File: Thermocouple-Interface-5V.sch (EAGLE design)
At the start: 16 parts, among them U1 MAX31855, U3 LP298XS

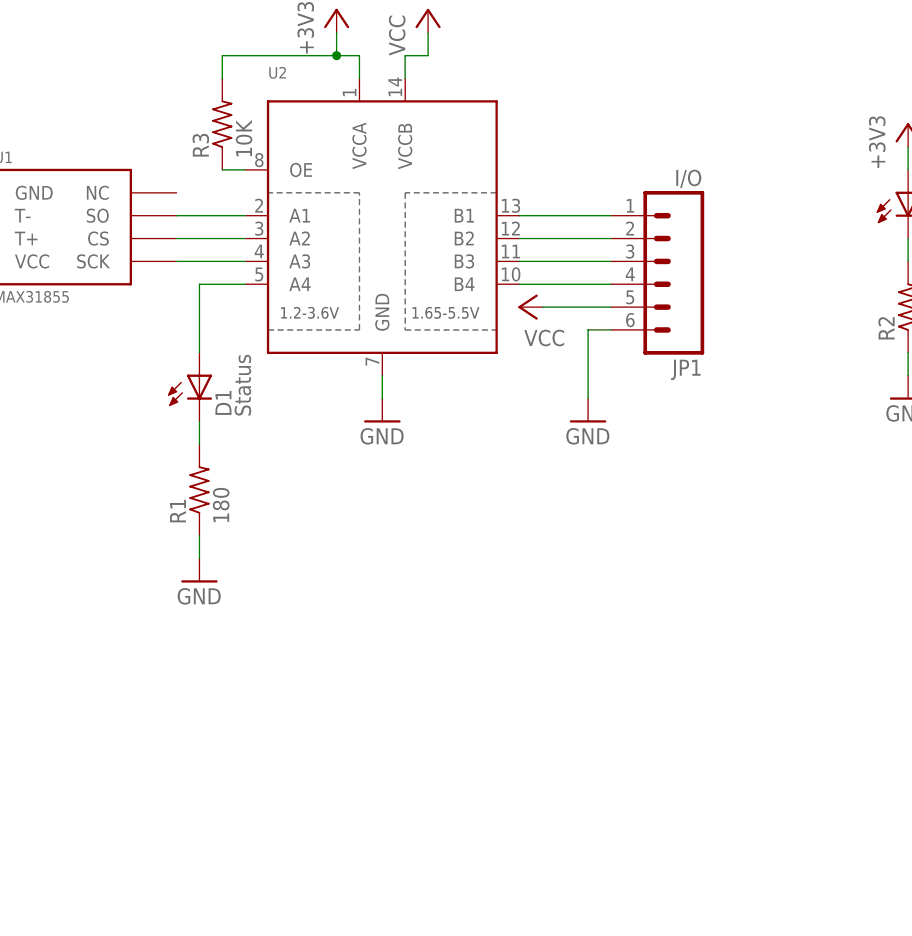
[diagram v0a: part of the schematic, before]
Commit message: Status led no longer routes through level shifter, bumped to v2.0.1 for 01-2012 pcb production
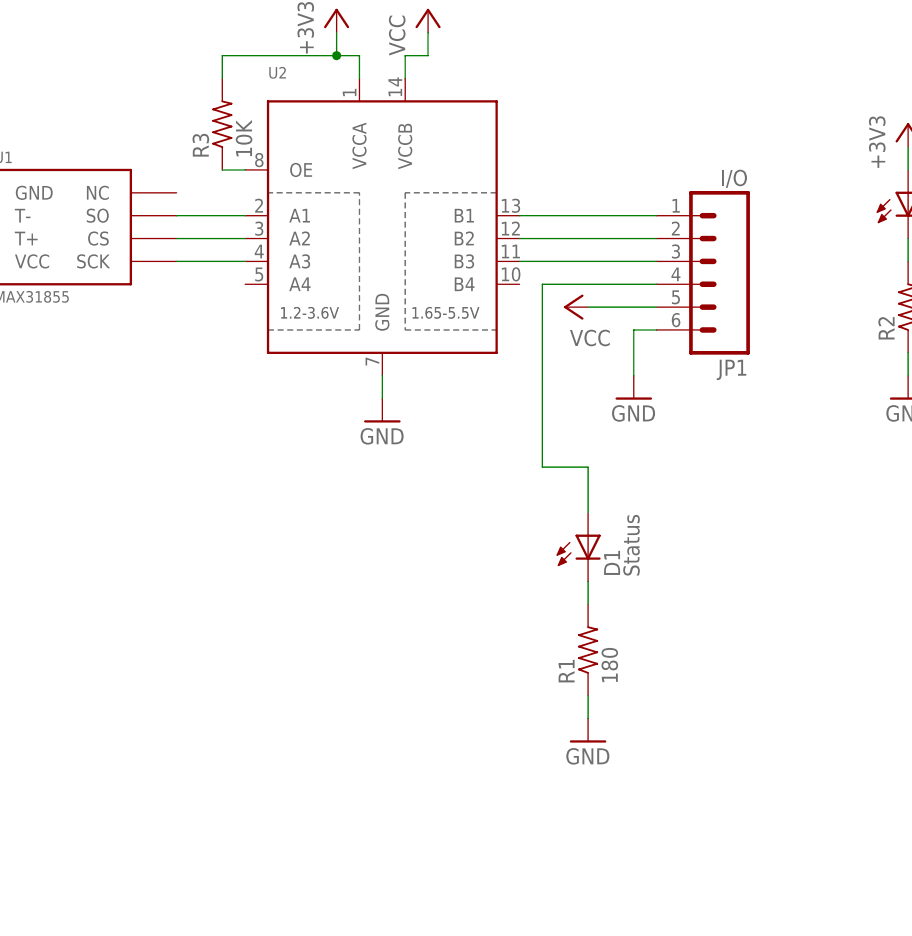
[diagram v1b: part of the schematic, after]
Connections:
- removed net STATUS: D1.A, U2.A4
- removed net _STATUS: JP1.4, U2.B4
- new net N$4: D1.A, JP1.4
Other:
- moved on the sheet: D1, JP1, R1
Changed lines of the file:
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@@
 <instance part="TC1" gate="G$1" x="78.74" y="124.46" rot="R180"/>
 <instance part="GND1" gate="1" x="93.98" y="104.14"/>
-<instance part="JP1" gate="G$1" x="185.42" y="119.38" rot="R180"/>
+<instance part="JP1" gate="G$1" x="190.5" y="119.38" rot="R180"/>
 <instance part="U$1" gate="G$1" x="15.24" y="15.24"/>
 <instance part="C1" gate="G$1" x="101.6" y="114.3"/>
-<instance part="+3V2" gate="G$1" x="170.18" y="114.3" rot="R90"/>
-<instance part="GND2" gate="1" x="177.8" y="101.6"/>
+<instance part="+3V2" gate="G$1" x="175.26" y="114.3" rot="R90"/>
+<instance part="GND2" gate="1" x="182.88" y="104.14"/>
 <instance part="GND3" gate="1" x="101.6" y="104.14"/>
 <instance part="U$2" gate="G$1" x="22.86" y="15.24"/>
-<instance part="D1" gate="G$1" x="134.62" y="106.68"/>
+<instance part="D1" gate="G$1" x="177.8" y="88.9"/>
 <instance part="D2" gate="G$1" x="213.36" y="127"/>
 <instance part="GND4" gate="1" x="213.36" y="104.14"/>
-<instance part="GND5" gate="1" x="134.62" y="83.82"/>
-<instance part="R1" gate="G$1" x="134.62" y="93.98" rot="R90"/>
+<instance part="GND5" gate="1" x="177.8" y="66.04"/>
+<instance part="R1" gate="G$1" x="177.8" y="76.2" rot="R90"/>
 <instance part="R2" gate="G$1" x="213.36" y="114.3" rot="R90"/>
 <instance part="U$3" gate="G$1" x="15.24" y="20.32"/>
@@
 </segment>
 <segment>
-<wire x1="180.34" y1="111.76" x2="177.8" y2="111.76" width="0.1524" layer="91"/>
-<wire x1="177.8" y1="111.76" x2="177.8" y2="104.14" width="0.1524" layer="91"/>
+<wire x1="185.42" y1="111.76" x2="182.88" y2="111.76" width="0.1524" layer="91"/>
+<wire x1="182.88" y1="111.76" x2="182.88" y2="106.68" width="0.1524" layer="91"/>
 <pinref part="GND2" gate="1" pin="GND"/>
 <pinref part="JP1" gate="G$1" pin="6"/>
@@
 </segment>
 <segment>
-<wire x1="134.62" y1="86.36" x2="134.62" y2="88.9" width="0.1524" layer="91"/>
+<wire x1="177.8" y1="68.58" x2="177.8" y2="71.12" width="0.1524" layer="91"/>
 <pinref part="GND5" gate="1" pin="GND"/>
 <pinref part="R1" gate="G$1" pin="1"/>
@@
 <net name="VCC" class="0">
 <segment>
-<wire x1="172.72" y1="114.3" x2="180.34" y2="114.3" width="0.1524" layer="91"/>
+<wire x1="177.8" y1="114.3" x2="185.42" y2="114.3" width="0.1524" layer="91"/>
 <pinref part="+3V2" gate="G$1" pin="+3V3"/>
 <pinref part="JP1" gate="G$1" pin="5"/>
@@
 <net name="N$1" class="0">
 <segment>
-<wire x1="134.62" y1="99.06" x2="134.62" y2="101.6" width="0.1524" layer="91"/>
+<wire x1="177.8" y1="81.28" x2="177.8" y2="83.82" width="0.1524" layer="91"/>
 <pinref part="R1" gate="G$1" pin="2"/>
 <pinref part="D1" gate="G$1" pin="C"/>
@@
 </segment>
 </net>
-<net name="STATUS" class="0">
-<segment>
-<wire x1="139.7" y1="116.84" x2="134.62" y2="116.84" width="0.1524" layer="91"/>
-<wire x1="134.62" y1="116.84" x2="134.62" y2="109.22" width="0.1524" layer="91"/>
-<pinref part="U2" gate="G$1" pin="A4"/>
-<pinref part="D1" gate="G$1" pin="A"/>
-</segment>
-</net>
 <net name="_SO" class="0">
 <segment>
-<wire x1="170.18" y1="124.46" x2="180.34" y2="124.46" width="0.1524" layer="91"/>
+<wire x1="170.18" y1="124.46" x2="185.42" y2="124.46" width="0.1524" layer="91"/>
 <pinref part="U2" gate="G$1" pin="B1"/>
 <pinref part="JP1" gate="G$1" pin="1"/>
@@
 <net name="_CS" class="0">
 <segment>
-<wire x1="170.18" y1="121.92" x2="180.34" y2="121.92" width="0.1524" layer="91"/>
+<wire x1="170.18" y1="121.92" x2="185.42" y2="121.92" width="0.1524" layer="91"/>
 <pinref part="U2" gate="G$1" pin="B2"/>
 <pinref part="JP1" gate="G$1" pin="2"/>
@@
 <net name="_SCK" class="0">
 <segment>
-<wire x1="170.18" y1="119.38" x2="180.34" y2="119.38" width="0.1524" layer="91"/>
+<wire x1="170.18" y1="119.38" x2="185.42" y2="119.38" width="0.1524" layer="91"/>
 <pinref part="U2" gate="G$1" pin="B3"/>
 <pinref part="JP1" gate="G$1" pin="3"/>
-</segment>
-</net>
-<net name="_STATUS" class="0">
-<segment>
-<wire x1="170.18" y1="116.84" x2="180.34" y2="116.84" width="0.1524" layer="91"/>
-<pinref part="U2" gate="G$1" pin="B4"/>
-<pinref part="JP1" gate="G$1" pin="4"/>
 </segment>
 </net>
@@
 </segment>
 </net>
+<net name="N$4" class="0">
+<segment>
+<pinref part="JP1" gate="G$1" pin="4"/>
+<wire x1="185.42" y1="116.84" x2="172.72" y2="116.84" width="0.1524" layer="91"/>
+<wire x1="172.72" y1="116.84" x2="172.72" y2="96.52" width="0.1524" layer="91"/>
+<pinref part="D1" gate="G$1" pin="A"/>
+<wire x1="172.72" y1="96.52" x2="177.8" y2="96.52" width="0.1524" layer="91"/>
+<wire x1="177.8" y1="96.52" x2="177.8" y2="91.44" width="0.1524" layer="91"/>
+</segment>
+</net>
